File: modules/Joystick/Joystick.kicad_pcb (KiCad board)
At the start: 2 copper layers, 40.6 x 40.6 mm, 7 parts, among them J1 Conn_01x10_Male, J2 Conn_01x10_Male

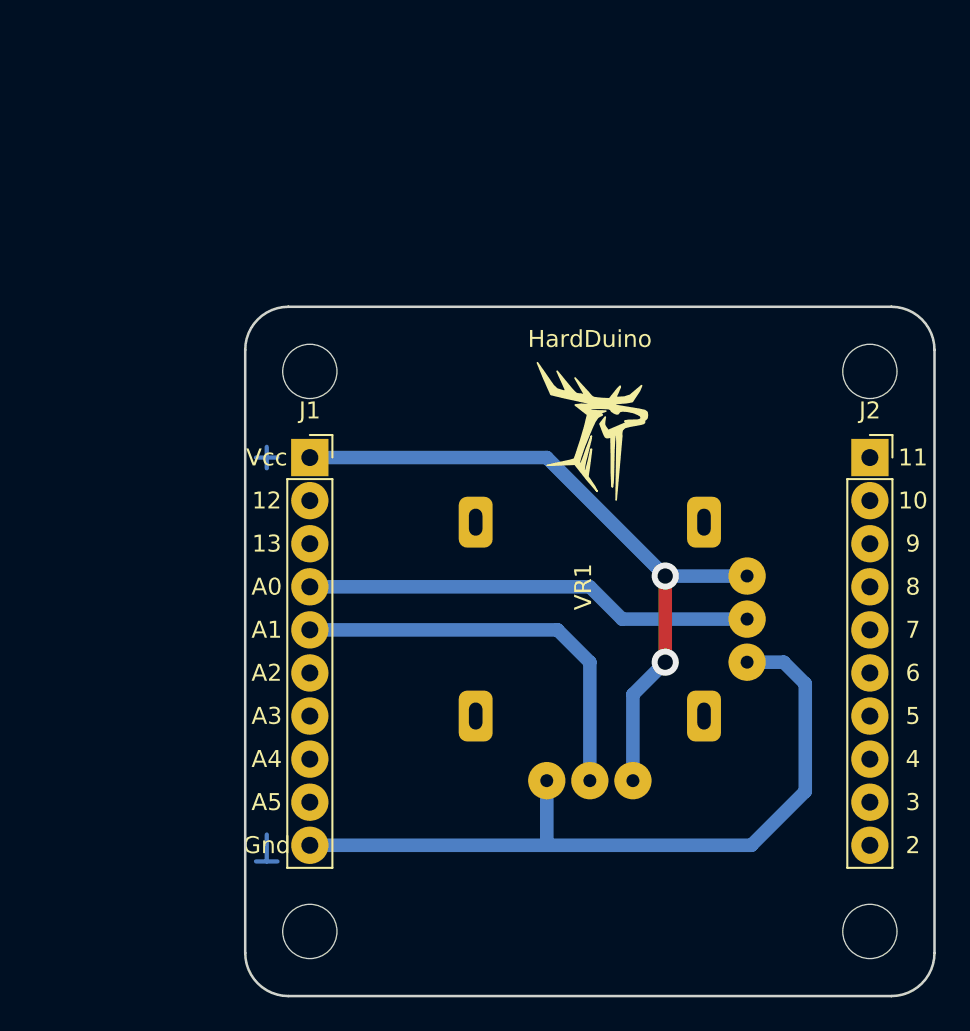
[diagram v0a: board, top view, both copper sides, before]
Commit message: 1x PCBs. Move holes to edges. Caution! This changes is uncompatible with previous versions...
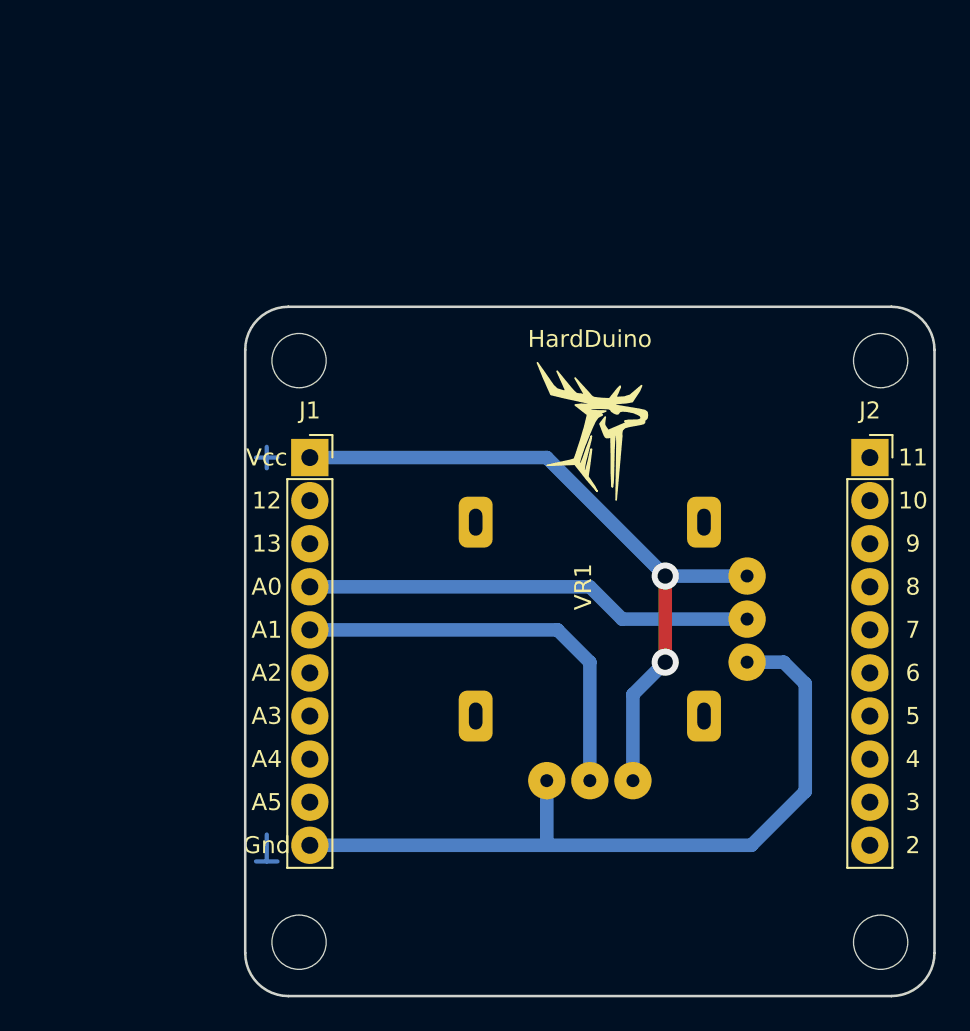
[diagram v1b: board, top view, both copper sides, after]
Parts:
- moved H2 0.90 mm to (92.1, 88.3)
- moved H4 0.90 mm to (126.4, 88.3)
- moved H1 0.90 mm to (92.1, 54.0)
- moved H3 0.90 mm to (126.4, 54.0)
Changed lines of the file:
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@@
   )
   (module MountingHole:MountingHole_3.2mm_M3 (layer F.Cu)
-    (at 92.71 54.61)
+    (at 92.0750 53.9750)
     (descr "Mounting Hole 3.2mm, no annular, M3")
     (tags "mounting hole 3.2mm no annular m3")
@@
   )
   (module MountingHole:MountingHole_3.2mm_M3 (layer F.Cu)
-    (at 92.71 87.63)
+    (at 92.0750 88.2650)
     (descr "Mounting Hole 3.2mm, no annular, M3")
     (tags "mounting hole 3.2mm no annular m3")
@@
   )
   (module MountingHole:MountingHole_3.2mm_M3 (layer F.Cu)
-    (at 125.73 54.61)
+    (at 126.3650 53.9750)
     (descr "Mounting Hole 3.2mm, no annular, M3")
     (tags "mounting hole 3.2mm no annular m3")
@@
   )
   (module MountingHole:MountingHole_3.2mm_M3 (layer F.Cu)
-    (at 125.73 87.63)
+    (at 126.3650 88.2650)
     (descr "Mounting Hole 3.2mm, no annular, M3")
     (tags "mounting hole 3.2mm no annular m3")

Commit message: Fix hash & version
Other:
- board text added: "21.02.2021"
- board text added: "b4d799"
- board text added: "v2.3"

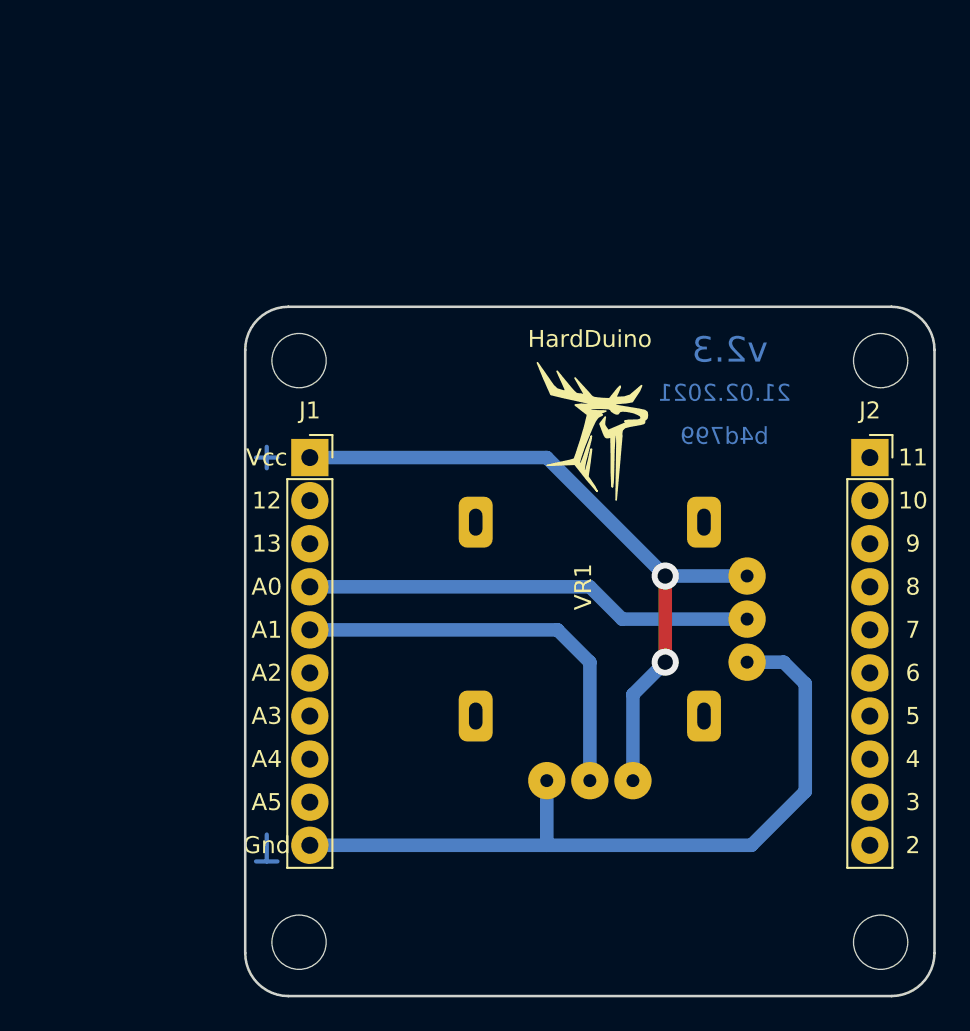
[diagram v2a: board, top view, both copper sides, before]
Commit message: All 1x shields was rotated clockwise
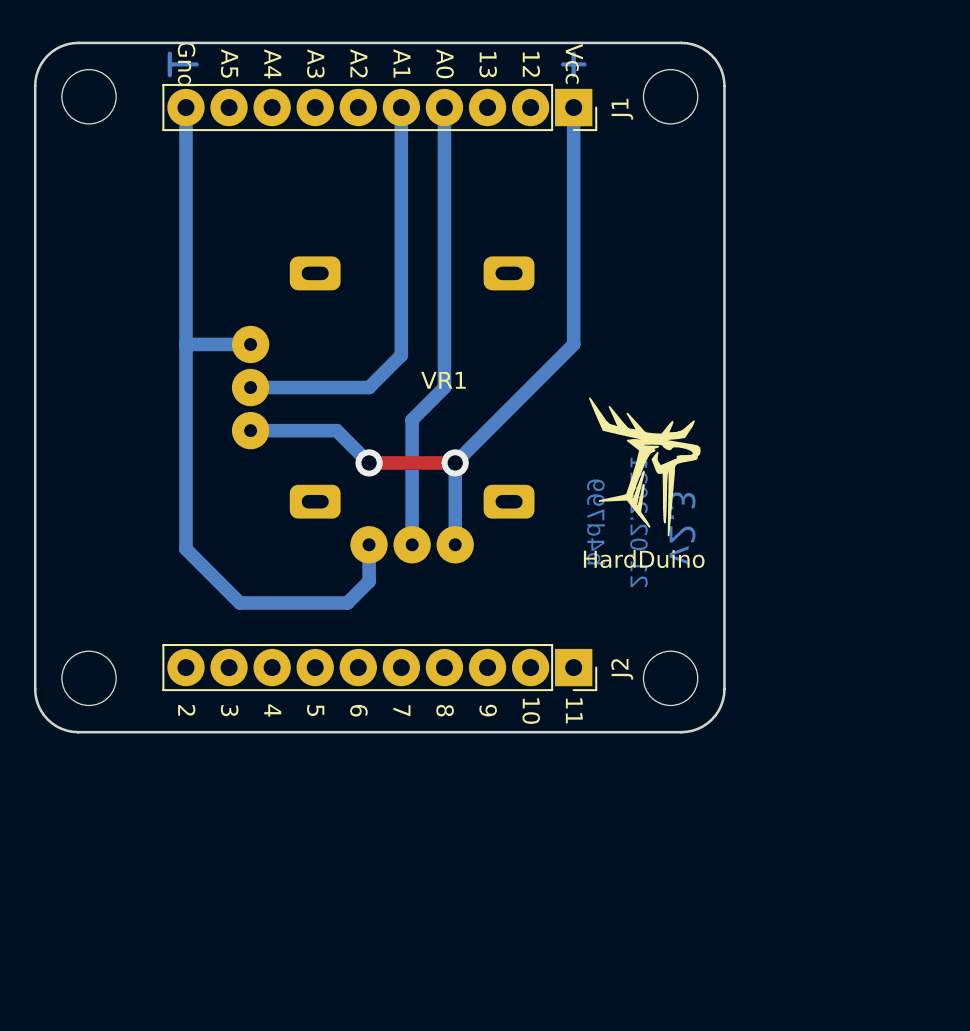
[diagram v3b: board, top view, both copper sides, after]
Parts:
- moved H2 51.4 mm to (79.7, 38.4), turned to 270 degrees
- moved H4 49.2 mm to (79.7, 72.7), turned to 270 degrees
- moved H1 26.9 mm to (114.0, 38.4), turned to 270 degrees
- moved J1 25.8 mm to (108.3, 39.1), turned to 270 degrees
- moved H3 22.5 mm to (114.0, 72.7), turned to 270 degrees
- moved J2 21.4 mm to (108.3, 72.1), turned to 270 degrees
- moved VR1 17.3 mm to (98.7, 55.3), turned to 0 degrees

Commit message: Now all mounting holes have distance 31.92 x 31.1
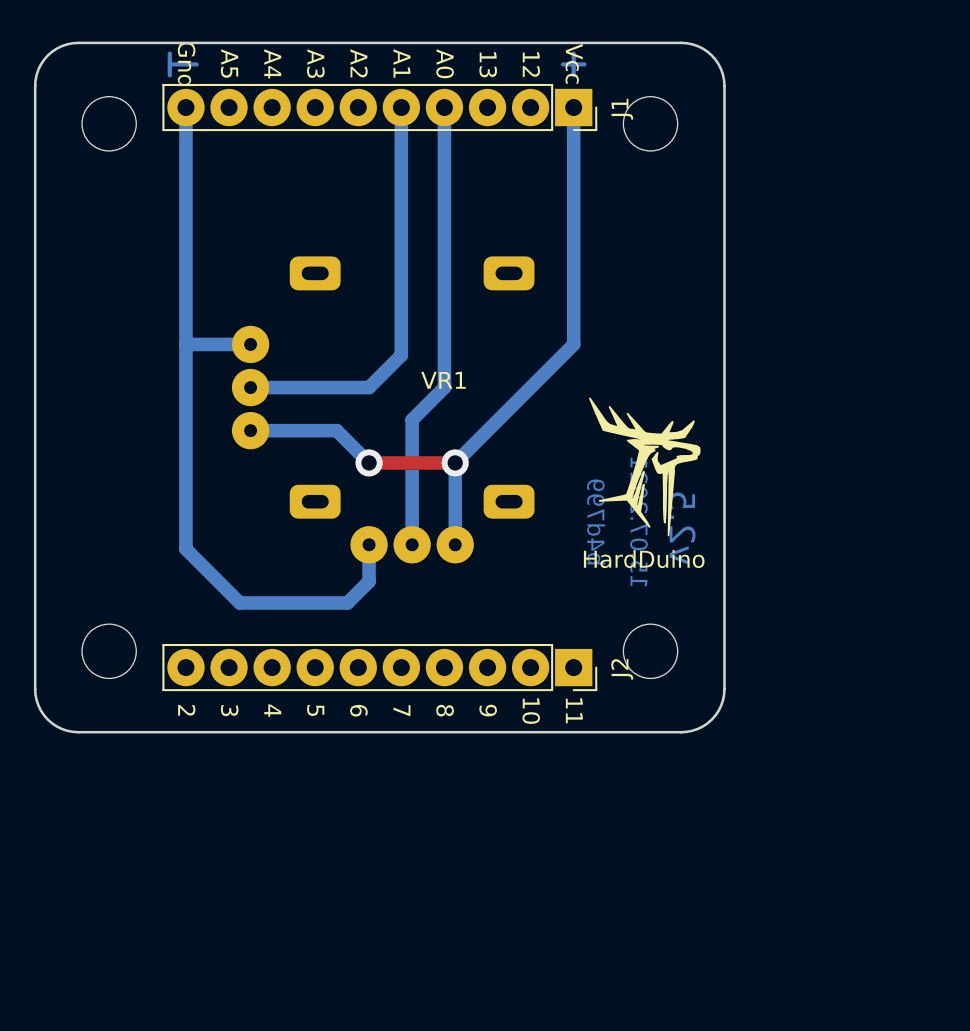
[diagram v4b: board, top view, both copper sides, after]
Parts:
- moved H1 1.99 mm to (112.8, 40.0), turned to 0 degrees
- moved H2 1.99 mm to (80.9, 40.0), turned to 0 degrees
- moved H3 1.99 mm to (112.8, 71.1), turned to 0 degrees
- moved H4 1.99 mm to (80.9, 71.1), turned to 0 degrees
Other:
- board text added: "15.07.2021"
- board text added: "v2.5"
- board text removed: "21.02.2021"
- board text removed: "v2.3"
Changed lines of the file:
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@@
   )
   (module MountingHole:MountingHole_3.2mm_M3 (layer F.Cu)
-    (at 113.9825 38.4175 270)
+    (at 112.7975 40.0125)
     (descr "Mounting Hole 3.2mm, no annular, M3")
     (tags "mounting hole 3.2mm no annular m3")
@@
       (effects (font (size 1 1) (thickness 0.15)))
     )
-    (fp_circle (center 0 0) (end 3.45 0) (layer F.CrtYd) (width 0.05))
-    (fp_circle (center 0 0) (end 3.2 0) (layer Cmts.User) (width 0.15))
+    (fp_circle (center 0 0) (end 3.2 0) (layer Cmts.User) (width 0.15))
+    (fp_circle (center 0 0) (end 3.45 0) (layer F.CrtYd) (width 0.05))
     (fp_text user %R (at 0.3 0 90) (layer F.Fab)
       (effects (font (size 1 1) (thickness 0.15)))
@@
   )
   (module MountingHole:MountingHole_3.2mm_M3 (layer F.Cu)
-    (at 79.6925 38.4175 270)
+    (at 80.8775 40.0125)
     (descr "Mounting Hole 3.2mm, no annular, M3")
     (tags "mounting hole 3.2mm no annular m3")
@@
       (effects (font (size 1 1) (thickness 0.15)))
     )
-    (fp_circle (center 0 0) (end 3.2 0) (layer Cmts.User) (width 0.15))
-    (fp_circle (center 0 0) (end 3.45 0) (layer F.CrtYd) (width 0.05))
+    (fp_circle (center 0 0) (end 3.45 0) (layer F.CrtYd) (width 0.05))
+    (fp_circle (center 0 0) (end 3.2 0) (layer Cmts.User) (width 0.15))
     (fp_text user %R (at 0.3 0 90) (layer F.Fab)
       (effects (font (size 1 1) (thickness 0.15)))
@@
   )
   (module MountingHole:MountingHole_3.2mm_M3 (layer F.Cu)
-    (at 113.9825 72.7075 270)
+    (at 112.7975 71.1125)
     (descr "Mounting Hole 3.2mm, no annular, M3")
     (tags "mounting hole 3.2mm no annular m3")
@@
       (effects (font (size 1 1) (thickness 0.15)))
     )
-    (fp_circle (center 0 0) (end 3.45 0) (layer F.CrtYd) (width 0.05))
-    (fp_circle (center 0 0) (end 3.2 0) (layer Cmts.User) (width 0.15))
+    (fp_circle (center 0 0) (end 3.2 0) (layer Cmts.User) (width 0.15))
+    (fp_circle (center 0 0) (end 3.45 0) (layer F.CrtYd) (width 0.05))
     (fp_text user %R (at 0.3 0 90) (layer F.Fab)
       (effects (font (size 1 1) (thickness 0.15)))
@@
   )
   (module MountingHole:MountingHole_3.2mm_M3 (layer F.Cu)
-    (at 79.6925 72.7075 270)
+    (at 80.8775 71.1125)
     (descr "Mounting Hole 3.2mm, no annular, M3")
     (tags "mounting hole 3.2mm no annular m3")
@@
       (effects (font (size 1 1) (thickness 0.15)))
     )
-    (fp_circle (center 0 0) (end 3.2 0) (layer Cmts.User) (width 0.15))
-    (fp_circle (center 0 0) (end 3.45 0) (layer F.CrtYd) (width 0.05))
+    (fp_circle (center 0 0) (end 3.45 0) (layer F.CrtYd) (width 0.05))
+    (fp_circle (center 0 0) (end 3.2 0) (layer Cmts.User) (width 0.15))
     (fp_text user %R (at 0 0 90) (layer F.Fab)
       (effects (font (size 1 1) (thickness 0.15)))
@@
       (effects (font (size 1 1) (thickness 0.15)))
     )
+    (fp_line (start -1.8 24.6) (end -1.8 -1.8) (layer F.CrtYd) (width 0.05))
+    (fp_line (start 1.75 24.6) (end -1.8 24.6) (layer F.CrtYd) (width 0.05))
+    (fp_line (start 1.75 -1.8) (end 1.75 24.6) (layer F.CrtYd) (width 0.05))
+    (fp_line (start -1.8 -1.8) (end 1.75 -1.8) (layer F.CrtYd) (width 0.05))
+    (fp_line (start 0 -1.33) (end 1.33 -1.33) (layer F.SilkS) (width 0.12))
+    (fp_line (start 1.33 -1.33) (end 1.33 0) (layer F.SilkS) (width 0.12))
+    (fp_line (start 1.33 1.27) (end 1.33 24.19) (layer F.SilkS) (width 0.12))
+    (fp_line (start -1.33 24.19) (end 1.33 24.19) (layer F.SilkS) (width 0.12))
+    (fp_line (start -1.33 1.27) (end -1.33 24.19) (layer F.SilkS) (width 0.12))
+    (fp_line (start -1.33 1.27) (end 1.33 1.27) (layer F.SilkS) (width 0.12))
+    (fp_line (start -1.27 24.13) (end -1.27 -1.27) (layer F.Fab) (width 0.1))
+    (fp_line (start 1.27 24.13) (end -1.27 24.13) (layer F.Fab) (width 0.1))
+    (fp_line (start 1.27 -0.635) (end 1.27 24.13) (layer F.Fab) (width 0.1))
+    (fp_line (start 0.635 -1.27) (end 1.27 -0.635) (layer F.Fab) (width 0.1))
     (fp_line (start -1.27 -1.27) (end 0.635 -1.27) (layer F.Fab) (width 0.1))
-    (fp_line (start 0.635 -1.27) (end 1.27 -0.635) (layer F.Fab) (width 0.1))
-    (fp_line (start 1.27 -0.635) (end 1.27 24.13) (layer F.Fab) (width 0.1))
-    (fp_line (start 1.27 24.13) (end -1.27 24.13) (layer F.Fab) (width 0.1))
-    (fp_line (start -1.27 24.13) (end -1.27 -1.27) (layer F.Fab) (width 0.1))
-    (fp_line (start -1.33 1.27) (end 1.33 1.27) (layer F.SilkS) (width 0.12))
-    (fp_line (start -1.33 1.27) (end -1.33 24.19) (layer F.SilkS) (width 0.12))
-    (fp_line (start -1.33 24.19) (end 1.33 24.19) (layer F.SilkS) (width 0.12))
-    (fp_line (start 1.33 1.27) (end 1.33 24.19) (layer F.SilkS) (width 0.12))
-    (fp_line (start 1.33 -1.33) (end 1.33 0) (layer F.SilkS) (width 0.12))
-    (fp_line (start 0 -1.33) (end 1.33 -1.33) (layer F.SilkS) (width 0.12))
-    (fp_line (start -1.8 -1.8) (end 1.75 -1.8) (layer F.CrtYd) (width 0.05))
-    (fp_line (start 1.75 -1.8) (end 1.75 24.6) (layer F.CrtYd) (width 0.05))
-    (fp_line (start 1.75 24.6) (end -1.8 24.6) (layer F.CrtYd) (width 0.05))
-    (fp_line (start -1.8 24.6) (end -1.8 -1.8) (layer F.CrtYd) (width 0.05))
     (fp_text user %R (at 0 11.43) (layer F.Fab)
       (effects (font (size 1 1) (thickness 0.15)))
@@
       (effects (font (size 1 1) (thickness 0.15)))
     )
+    (fp_line (start -1.27 -1.27) (end 0.635 -1.27) (layer F.Fab) (width 0.1))
+    (fp_line (start 0.635 -1.27) (end 1.27 -0.635) (layer F.Fab) (width 0.1))
+    (fp_line (start 1.27 -0.635) (end 1.27 24.13) (layer F.Fab) (width 0.1))
+    (fp_line (start 1.27 24.13) (end -1.27 24.13) (layer F.Fab) (width 0.1))
+    (fp_line (start -1.27 24.13) (end -1.27 -1.27) (layer F.Fab) (width 0.1))
+    (fp_line (start -1.33 1.27) (end 1.33 1.27) (layer F.SilkS) (width 0.12))
+    (fp_line (start -1.33 1.27) (end -1.33 24.19) (layer F.SilkS) (width 0.12))
+    (fp_line (start -1.33 24.19) (end 1.33 24.19) (layer F.SilkS) (width 0.12))
+    (fp_line (start 1.33 1.27) (end 1.33 24.19) (layer F.SilkS) (width 0.12))
+    (fp_line (start 1.33 -1.33) (end 1.33 0) (layer F.SilkS) (width 0.12))
+    (fp_line (start 0 -1.33) (end 1.33 -1.33) (layer F.SilkS) (width 0.12))
+    (fp_line (start -1.8 -1.8) (end 1.75 -1.8) (layer F.CrtYd) (width 0.05))
+    (fp_line (start 1.75 -1.8) (end 1.75 24.6) (layer F.CrtYd) (width 0.05))
+    (fp_line (start 1.75 24.6) (end -1.8 24.6) (layer F.CrtYd) (width 0.05))
     (fp_line (start -1.8 24.6) (end -1.8 -1.8) (layer F.CrtYd) (width 0.05))
-    (fp_line (start 1.75 24.6) (end -1.8 24.6) (layer F.CrtYd) (width 0.05))
-    (fp_line (start 1.75 -1.8) (end 1.75 24.6) (layer F.CrtYd) (width 0.05))
-    (fp_line (start -1.8 -1.8) (end 1.75 -1.8) (layer F.CrtYd) (width 0.05))
-    (fp_line (start 0 -1.33) (end 1.33 -1.33) (layer F.SilkS) (width 0.12))
-    (fp_line (start 1.33 -1.33) (end 1.33 0) (layer F.SilkS) (width 0.12))
-    (fp_line (start 1.33 1.27) (end 1.33 24.19) (layer F.SilkS) (width 0.12))
-    (fp_line (start -1.33 24.19) (end 1.33 24.19) (layer F.SilkS) (width 0.12))
-    (fp_line (start -1.33 1.27) (end -1.33 24.19) (layer F.SilkS) (width 0.12))
-    (fp_line (start -1.33 1.27) (end 1.33 1.27) (layer F.SilkS) (width 0.12))
-    (fp_line (start -1.27 24.13) (end -1.27 -1.27) (layer F.Fab) (width 0.1))
-    (fp_line (start 1.27 24.13) (end -1.27 24.13) (layer F.Fab) (width 0.1))
-    (fp_line (start 1.27 -0.635) (end 1.27 24.13) (layer F.Fab) (width 0.1))
-    (fp_line (start 0.635 -1.27) (end 1.27 -0.635) (layer F.Fab) (width 0.1))
-    (fp_line (start -1.27 -1.27) (end 0.635 -1.27) (layer F.Fab) (width 0.1))
     (fp_text user %R (at 0 11.43) (layer F.Fab)
       (effects (font (size 1 1) (thickness 0.15)))
@@
     (effects (font (size 1 1) (thickness 0.2)) (justify mirror))
   )
-  (gr_text 21.02.2021 (at 112.0775 63.5 270) (layer B.Cu)
+  (gr_text 15.07.2021 (at 112.0775 63.5 270) (layer B.Cu)
     (effects (font (size 1 1) (thickness 0.2)) (justify mirror))
   )
-  (gr_text v2.3 (at 114.6175 63.8175 270) (layer B.Cu)
+  (gr_text v2.5 (at 114.6175 63.8175 270) (layer B.Cu)
     (effects (font (size 1.5 1.5) (thickness 0.3)) (justify mirror))
   )
